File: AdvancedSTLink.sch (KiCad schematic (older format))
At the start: 53 parts, among them J1 USB_C_Receptacle, J2 Conn_02x03_Odd_Even, J3 Conn_01x06, J4 Conn_02x03_Odd_Even, SW1 SW_SPDT, U1 STM32F205RETx, U2 XC6206P332MR, U3 USBLC6-2P6, U4 MP2359, U5 USBLC6-2P6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

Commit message: DRC fixes
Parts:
- added C15: 100nF, Capacitor_SMD:C_0402_1005Metric, symbol Device:C_Small
- J3: symbol Connector_Generic:Conn_01x06 -> Connector_Generic_MountingPin:Conn_01x06_MountingPin
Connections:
- net GND: now also J3.MP (MountPin), C15.2
- net V_OUT_3.3: now also C15.1
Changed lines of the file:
@@
 $EndComp
 $Comp
-L Connector_Generic:Conn_01x06 J3
+L Connector_Generic_MountingPin:Conn_01x06_MountingPin J3
 U 1 1 5E9ED5E8
 P 9150 2200
@@
 	-1   0    0    1
 $EndComp
+$Comp
+L Device:C_Small C15
+U 1 1 5EE35A85
+P 10000 2250
+F 0 "C15" H 10092 2296 50  0000 L CNN
+F 1 "100nF" H 10092 2205 50  0000 L CNN
+F 2 "Capacitor_SMD:C_0402_1005Metric" H 10000 2250 50  0001 C CNN
+F 3 "~" H 10000 2250 50  0001 C CNN
+	1    10000 2250
+	1    0    0    -1
+$EndComp
+$Comp
+L power:GND #PWR0101
+U 1 1 5EE35A8F
+P 10000 2350
+F 0 "#PWR0101" H 10000 2100 50  0001 C CNN
+F 1 "GND" H 10005 2177 50  0000 C CNN
+F 2 "" H 10000 2350 50  0001 C CNN
+F 3 "" H 10000 2350 50  0001 C CNN
+	1    10000 2350
+	1    0    0    -1
+$EndComp
+Text GLabel 10000 2150 1    50   Input ~ 0
+V_OUT_3.3
+$Comp
+L power:GND #PWR?
+U 1 1 5EE6A2B9
+P 9150 2700
+F 0 "#PWR?" H 9150 2450 50  0001 C CNN
+F 1 "GND" H 9155 2527 50  0000 C CNN
+F 2 "" H 9150 2700 50  0001 C CNN
+F 3 "" H 9150 2700 50  0001 C CNN
+	1    9150 2700
+	1    0    0    -1
+$EndComp
 $EndSCHEMATC

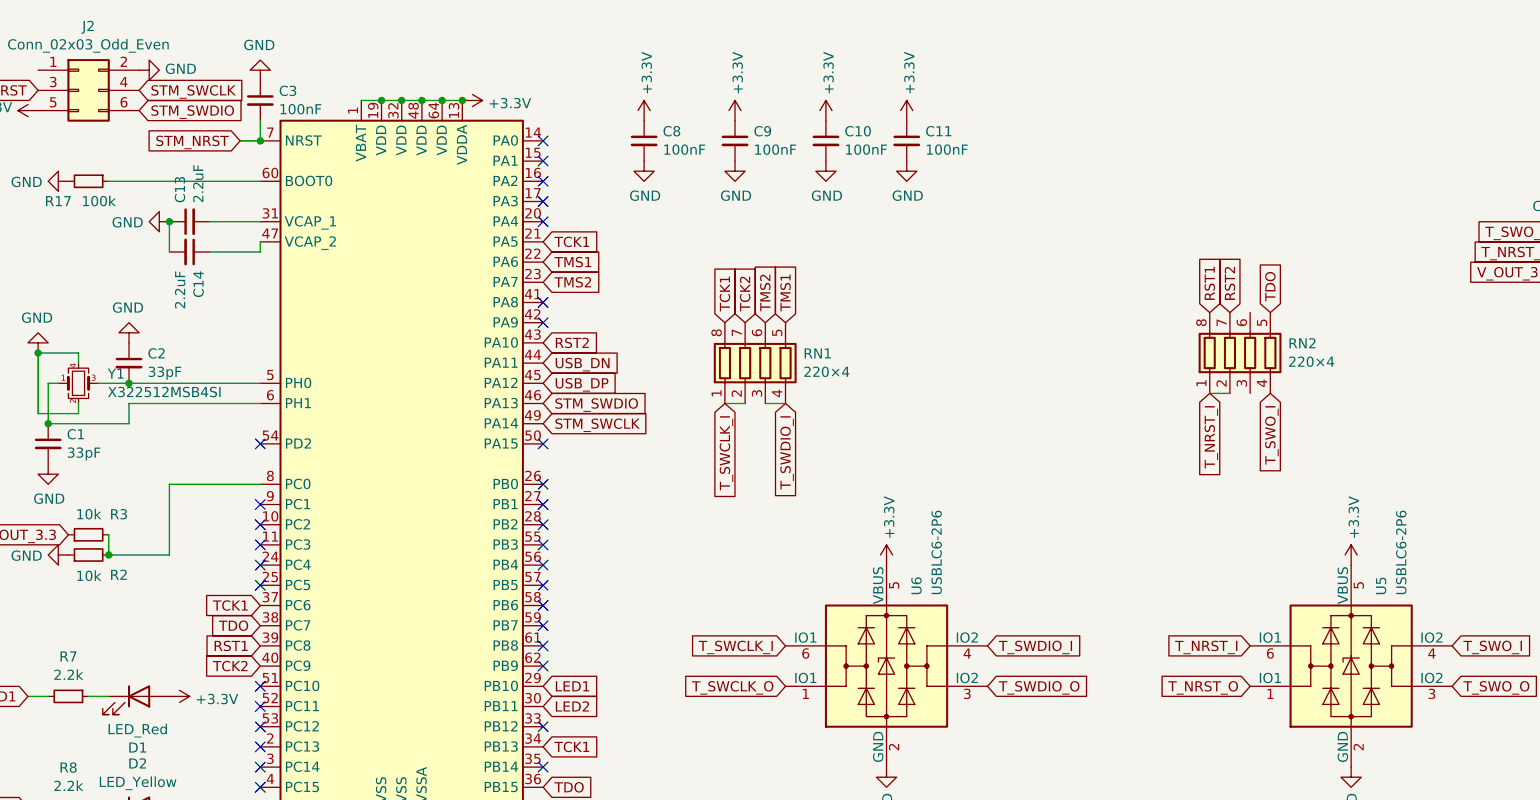
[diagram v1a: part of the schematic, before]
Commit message: Rearrange RST.
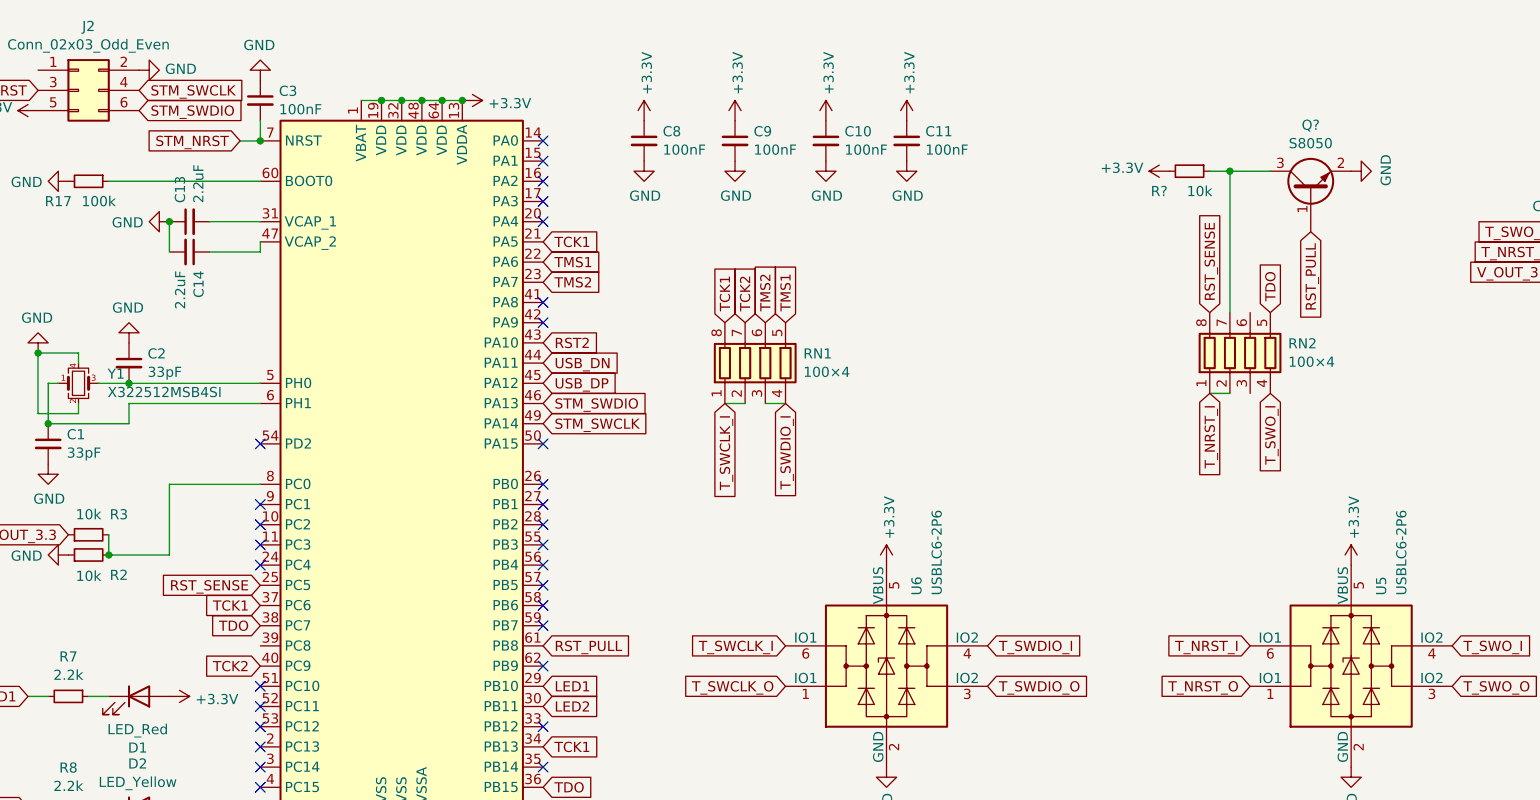
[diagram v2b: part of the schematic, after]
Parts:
- added Q?: S8050, lc:SOT-23(SOT-23-3), symbol Transistor_BJT:MMBT3904
- added R?: 10k, Resistor_SMD:R_0402_1005Metric, symbol Device:R_Small
- RN1, RN2: value 220×4 -> 100×4
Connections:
- net +3V3: now also R?.2
- net GND: now also Q?.2 (E)
- net RST2: no longer RN2.7 (R2.2)
- net RST_SENSE: now reaches U1.25 (PC5)
- net RST_SENSE: now also RN2.8 (R1.2)
- net RST_PULL: now reaches U1.61 (PB8)
- net RST_PULL: now also Q?.1 (B)
- net RST1: no longer names the net of U1.39 (PC8)
- net RST1: no longer RN2.8 (R1.2)
- new net: Q?.3 (C), R?.1, RN2.7 (R2.2)
- no-connect marks 32 -> 30
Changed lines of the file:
@@
 NoConn ~ 2100 3100
 NoConn ~ 2100 3200
-NoConn ~ 2100 3300
 Text GLabel 2100 3400 0    50   Input ~ 0
 TCK1
@@
 Text GLabel 3500 4300 2    50   Input ~ 0
 TDO
-Text GLabel 2100 3600 0    50   Input ~ 0
-RST1
+Text GLabel 2100 3300 0    50   Input ~ 0
+RST_SENSE
 NoConn ~ 2100 3800
 NoConn ~ 2100 3900
@@
 NoConn ~ 3500 3400
 NoConn ~ 3500 3500
-NoConn ~ 3500 3600
 NoConn ~ 3500 3700
 NoConn ~ 3500 4000
@@
 	0    1    1    0
 $EndComp
-Text GLabel 6900 1950 1    50   Input ~ 0
-RST2
-Text GLabel 6800 1950 1    50   Input ~ 0
-RST1
 $Comp
 L Switch:SW_SPDT SW1
@@
 P 4600 2200
 F 0 "RN1" H 4788 2246 50  0000 L CNN
-F 1 "220×4" H 4788 2155 50  0000 L CNN
+F 1 "100×4" H 4788 2155 50  0000 L CNN
 F 2 "lc:0402_RX4" V 4875 2200 50  0001 C CNN
 F 3 "~" H 4600 2200 50  0001 C CNN
@@
 P 7000 2150
 F 0 "RN2" H 7188 2196 50  0000 L CNN
-F 1 "220×4" H 7188 2105 50  0000 L CNN
+F 1 "100×4" H 7188 2105 50  0000 L CNN
 F 2 "lc:0402_RX4" V 7275 2150 50  0001 C CNN
 F 3 "~" H 7000 2150 50  0001 C CNN
@@
 	1    0    0    -1
 $EndComp
+Text GLabel 3500 3600 2    50   Input ~ 0
+RST_PULL
+Text GLabel 6800 1950 1    50   Input ~ 0
+RST_SENSE
+$Comp
+L Transistor_BJT:MMBT3904 Q?
+U 1 1 5EE60005
+P 7300 1350
+F 0 "Q?" V 7628 1350 50  0000 C CNN
+F 1 "S8050" V 7537 1350 50  0000 C CNN
+F 2 "lc:SOT-23(SOT-23-3)" H 7500 1275 50  0001 L CIN
+F 3 "" H 7300 1350 50  0001 L CNN
+	1    7300 1350
+	0    -1   -1   0
+$EndComp
+Text GLabel 7300 1550 3    50   Input ~ 0
+RST_PULL
+Wire Wire Line
+	7100 1250 6900 1250
+Wire Wire Line
+	6900 1250 6900 1950
+$Comp
+L Device:R_Small R?
+U 1 1 5EE6578A
+P 6700 1250
+F 0 "R?" V 6800 1100 50  0000 C CNN
+F 1 "10k" V 6800 1300 50  0000 C CNN
+F 2 "Resistor_SMD:R_0402_1005Metric" H 6700 1250 50  0001 C CNN
+F 3 "~" H 6700 1250 50  0001 C CNN
+	1    6700 1250
+	0    1    1    0
+$EndComp
+Wire Wire Line
+	6800 1250 6900 1250
+Connection ~ 6900 1250
+$Comp
+L power:+3.3V #PWR?
+U 1 1 5EE68E5B
+P 6600 1250
+F 0 "#PWR?" H 6600 1100 50  0001 C CNN
+F 1 "+3.3V" V 6615 1378 50  0000 L CNN
+F 2 "" H 6600 1250 50  0001 C CNN
+F 3 "" H 6600 1250 50  0001 C CNN
+	1    6600 1250
+	0    -1   -1   0
+$EndComp
+$Comp
+L power:GND #PWR?
+U 1 1 5EE69600
+P 7500 1250
+F 0 "#PWR?" H 7500 1000 50  0001 C CNN
+F 1 "GND" H 7505 1077 50  0000 C CNN
+F 2 "" H 7500 1250 50  0001 C CNN
+F 3 "" H 7500 1250 50  0001 C CNN
+	1    7500 1250
+	0    -1   -1   0
+$EndComp
 $EndSCHEMATC

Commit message: Sch.
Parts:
- U2: footprint lc:SOT-23-3L -> lc:SOT-23(SOT-23-3)
- gave numbers to parts that had none: 2
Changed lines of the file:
@@
 F 0 "U2" H 3000 7392 50  0000 C CNN
 F 1 "XC6206P332MR" H 3000 7301 50  0000 C CNN
-F 2 "lc:SOT-23-3L" H 3000 7375 50  0001 C CIN
+F 2 "lc:SOT-23(SOT-23-3)" H 3000 7375 50  0001 C CIN
 F 3 "https://www.torexsemi.com/file/xc6206/XC6206.pdf" H 3000 7150 50  0001 C CNN
 	1    3000 7150
@@
 V_OUT_3.3
 $Comp
-L power:GND #PWR?
+L power:GND #PWR0111
 U 1 1 5EE6A2B9
 P 9150 2700
-F 0 "#PWR?" H 9150 2450 50  0001 C CNN
+F 0 "#PWR0111" H 9150 2450 50  0001 C CNN
 F 1 "GND" H 9155 2527 50  0000 C CNN
 F 2 "" H 9150 2700 50  0001 C CNN
@@
 RST_SENSE
 $Comp
-L Transistor_BJT:MMBT3904 Q?
+L Transistor_BJT:MMBT3904 Q1
 U 1 1 5EE60005
 P 7300 1350
-F 0 "Q?" V 7628 1350 50  0000 C CNN
+F 0 "Q1" V 7628 1350 50  0000 C CNN
 F 1 "S8050" V 7537 1350 50  0000 C CNN
 F 2 "lc:SOT-23(SOT-23-3)" H 7500 1275 50  0001 L CIN
@@
 	6900 1250 6900 1950
 $Comp
-L Device:R_Small R?
+L Device:R_Small R6
 U 1 1 5EE6578A
 P 6700 1250
-F 0 "R?" V 6800 1100 50  0000 C CNN
+F 0 "R6" V 6800 1100 50  0000 C CNN
 F 1 "10k" V 6800 1300 50  0000 C CNN
 F 2 "Resistor_SMD:R_0402_1005Metric" H 6700 1250 50  0001 C CNN
@@
 Connection ~ 6900 1250
 $Comp
-L power:+3.3V #PWR?
+L power:+3.3V #PWR0112
 U 1 1 5EE68E5B
 P 6600 1250
-F 0 "#PWR?" H 6600 1100 50  0001 C CNN
+F 0 "#PWR0112" H 6600 1100 50  0001 C CNN
 F 1 "+3.3V" V 6615 1378 50  0000 L CNN
 F 2 "" H 6600 1250 50  0001 C CNN
@@
 $EndComp
 $Comp
-L power:GND #PWR?
+L power:GND #PWR0113
 U 1 1 5EE69600
 P 7500 1250
-F 0 "#PWR?" H 7500 1000 50  0001 C CNN
+F 0 "#PWR0113" H 7500 1000 50  0001 C CNN
 F 1 "GND" H 7505 1077 50  0000 C CNN
 F 2 "" H 7500 1250 50  0001 C CNN

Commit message: correct fabrication version
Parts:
- FB1: footprint Inductor_SMD:L_0603_1608Metric -> Inductor_SMD:L_0805_2012Metric
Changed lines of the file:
@@
 F 0 "FB1" V 2413 4900 50  0000 C CNN
 F 1 "Ferrite_Bead_Small" V 2504 4900 50  0000 C CNN
-F 2 "Inductor_SMD:L_0603_1608Metric" V 2580 4900 50  0001 C CNN
+F 2 "Inductor_SMD:L_0805_2012Metric" V 2580 4900 50  0001 C CNN
 F 3 "~" H 2650 4900 50  0001 C CNN
 	1    2650 4900
